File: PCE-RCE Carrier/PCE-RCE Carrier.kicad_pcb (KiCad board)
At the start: 2 copper layers, 38 x 39.5 mm, 35 parts, among them J10 Conn_01x06_Pin, J11 Conn_01x02, J2 XT60PW-F, J3 XT30UPB-M, J4 XT60PW-F, J5 DF40C-34DP-0.4V_58_, J6 PRT-16766, J7 DF40C-34DP-0.4V_58_, J9 XT30UPB-M, U2 TPS54302DDCR, U3 BD6222HFP-TR, U4 LMR51430, U5 BD6222HFP-TR

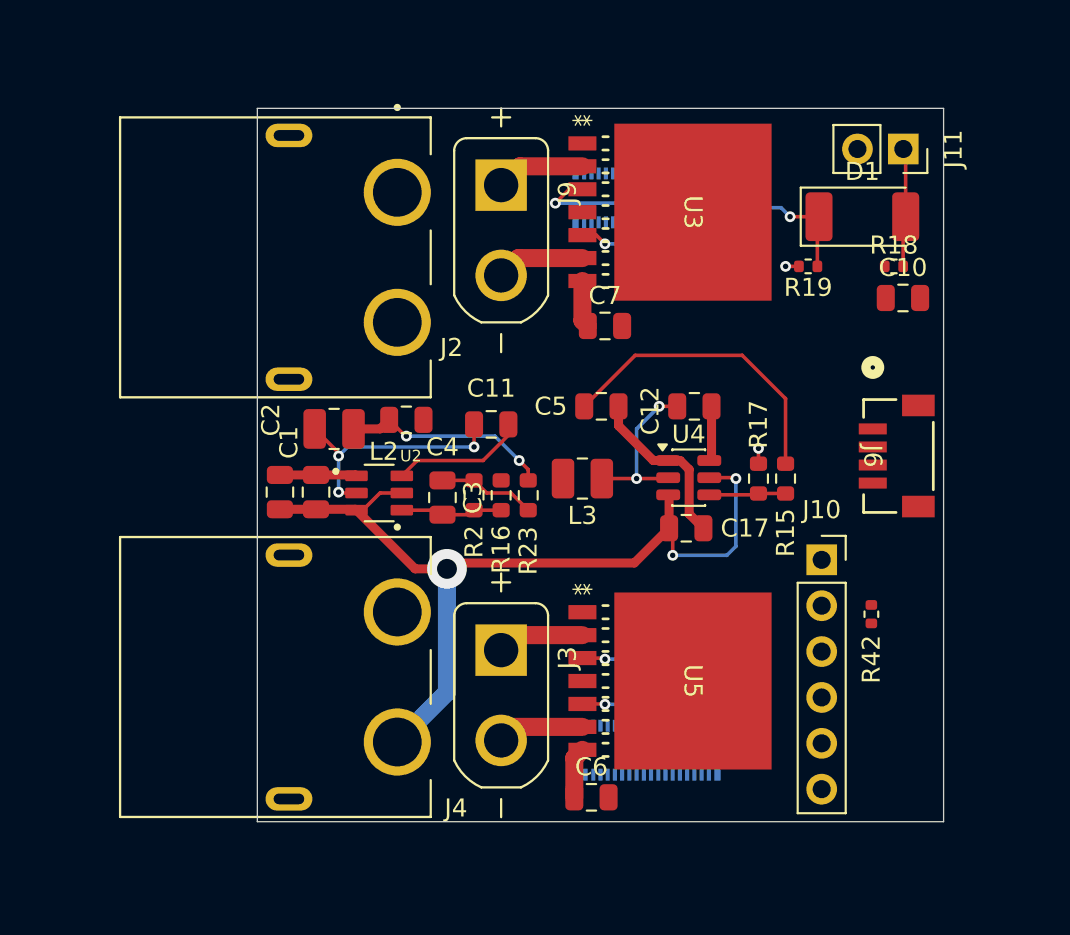
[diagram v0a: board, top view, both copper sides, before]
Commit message: PCE wiring except solenoids and 3V3 in
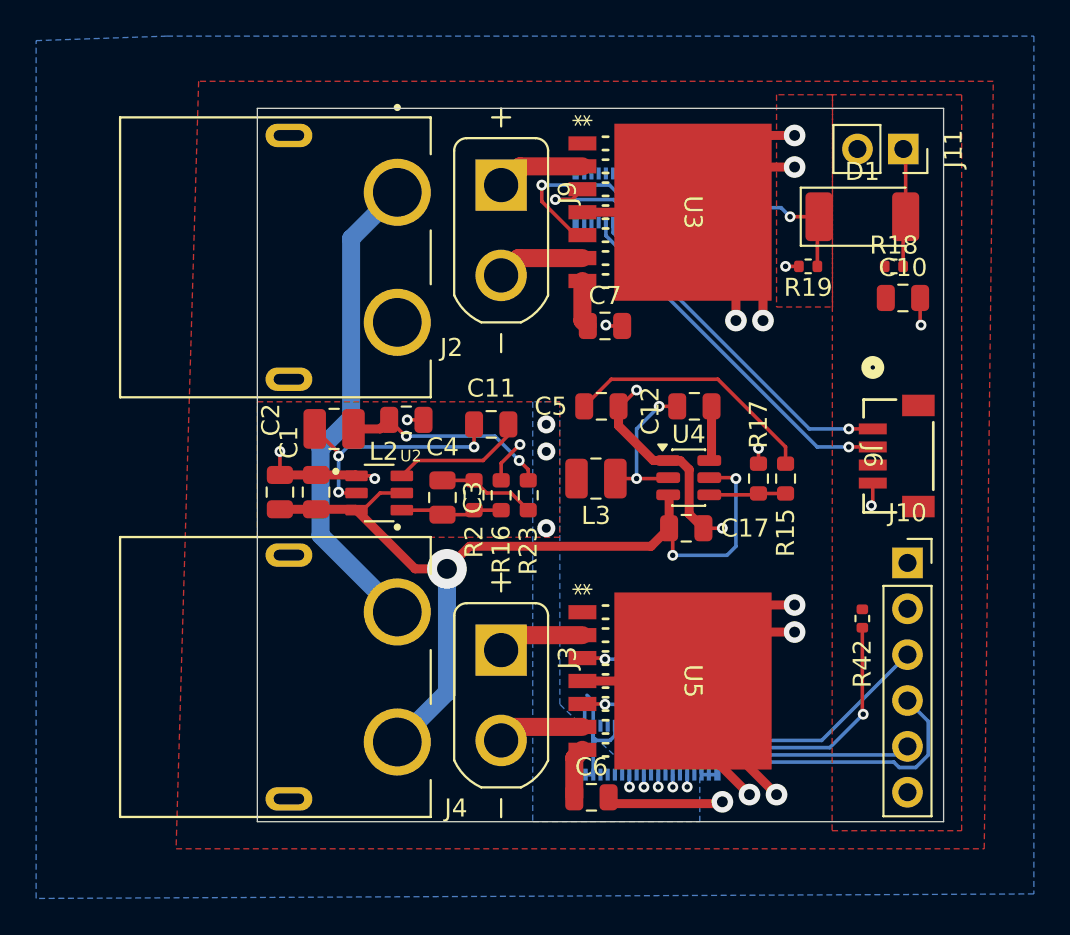
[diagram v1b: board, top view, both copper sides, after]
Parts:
- moved J10 4.75 mm to (158.0, 79.2)
- moved L3 0.75 mm to (140.8, 74.5)
- moved R42 0.55 mm to (155.5, 82.2)
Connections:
- C10 pad 1: +3.3V -> +3V3
- J4 pad S1: unconnected-(J4-SHIELD-PadS1) -> GND
- J4 pad S2: unconnected-(J4-SHIELD-PadS1)_1 -> GND
- J7 pad 16: unconnected-(J7-Pad16) -> +3V3_REG
- J7 pad 20: unconnected-(J7-Pad20) -> +3V3_REG
- J7 pad 24: unconnected-(J7-Pad24) -> +3V3_REG
- J7 pad 25: /PYRO_5 -> unconnected-(J7-Pad25)
- J7 pad 27: /PYRO_4 -> unconnected-(J7-Pad27)
- J7 pad 28: unconnected-(J7-Pad28) -> +3V3_REG
- J7 pad 29: /PYRO_3 -> unconnected-(J7-Pad29)
- J7 pad 31: /PYRO_2 -> unconnected-(J7-Pad31)
- J7 pad 33: /PYRO_1 -> unconnected-(J7-Pad33)
- R18 pad 1: +3.3V -> +3V3
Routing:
- net GND: track 15.4 -> 116.5 mm, vias 2 -> 20
- net /Power Distribution and Motor Control/VBAT: track 0.00 -> 26.8 mm
- net /SPI_CS: track 0.00 -> 22.3 mm
- net /SDA: track 0.00 -> 20.4 mm, vias 0 -> 1
- net /SCL: track 0.00 -> 19.4 mm, vias 0 -> 1
- net /MISO: track 0.00 -> 19.0 mm, vias 0 -> 1
- net /MOSI: track 0.00 -> 17.2 mm
- net /SCLK: track 0.00 -> 16.8 mm
- net /PAYLOAD_1R: track 3.91 -> 10.3 mm
- net +3V3_REG: track 11.6 -> 15.0 mm, vias 2 -> 10
- net +12V: track 22.3 -> 19.7 mm
- net Net-(U4-SW): track 9.21 -> 8.46 mm
- added copper zone on F.Cu, net +12V
- added copper zone on F.Cu, net +3V3
- added copper zone on B.Cu, net +3V3_REG
- added copper zone on F.Cu, net +3V3_REG
- added copper zone on B.Cu, net GND

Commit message: added payload solenoid gpio, 3v3 rail from power mux to carriers, finished wiring
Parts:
- added J1: Conn_01x02, Connector_PinHeader_2.54mm:PinHeader_1x02_P2.54mm_Vertical, F.Cu at (134.2, 68.0)
- added Q1: SP2002KNC, Package_DFN_QFN:Diodes_DFN1006-3, F.Cu at (139.8, 68.0)
- added R1: 10k, Resistor_SMD:R_0402_1005Metric, F.Cu at (141.7, 68.2)
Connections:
- J5 pad 3: unconnected-(J5-Pad3) -> +3V3
- J5 pad 4: unconnected-(J5-Pad4) -> /PAYLOAD_S
- J5 pad 7: +3V3_REG -> +3V3
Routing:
- net +3V3: track 0.00 -> 18.6 mm, vias 0 -> 2
- net /PAYLOAD_S: track 0.00 -> 9.29 mm, vias 0 -> 1
- net GND: track 116.5 -> 124.5 mm, vias 20 -> 22
- net Net-(J1-Pin_2): track 0.00 -> 2.74 mm
